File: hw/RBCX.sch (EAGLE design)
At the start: 477 parts, among them IC1 AMS1117-3.3, IC10 INA180A4, IC11 INA180A4, IC12 MPU-6050, IC13 STM32F103VCT6, IC2 DRV8833PWP, IC3 INA180A4, IC4 INA180A4, IC5 DRV8833PWP, IC6 INA180A4, IC7 INA180A4, IC8 INA180A4, IC9 INA180A4, P1 M1, P2 M2, P3 M3, P4 M4, Q1 NCE20P45Q, Q10 2N7002, Q2 NCE20P45Q, Q3 2N7002, Q4 2N7002, Q5 2N7002, Q6 2N7002, Q7 2N7002, Q8 2N7002, Q9 2N7002, X1 POWER_IN, X2 POWER_OUT, X3 52559-3092, X4 uUSB, Y1 5032/2P, Y2 3215_2P

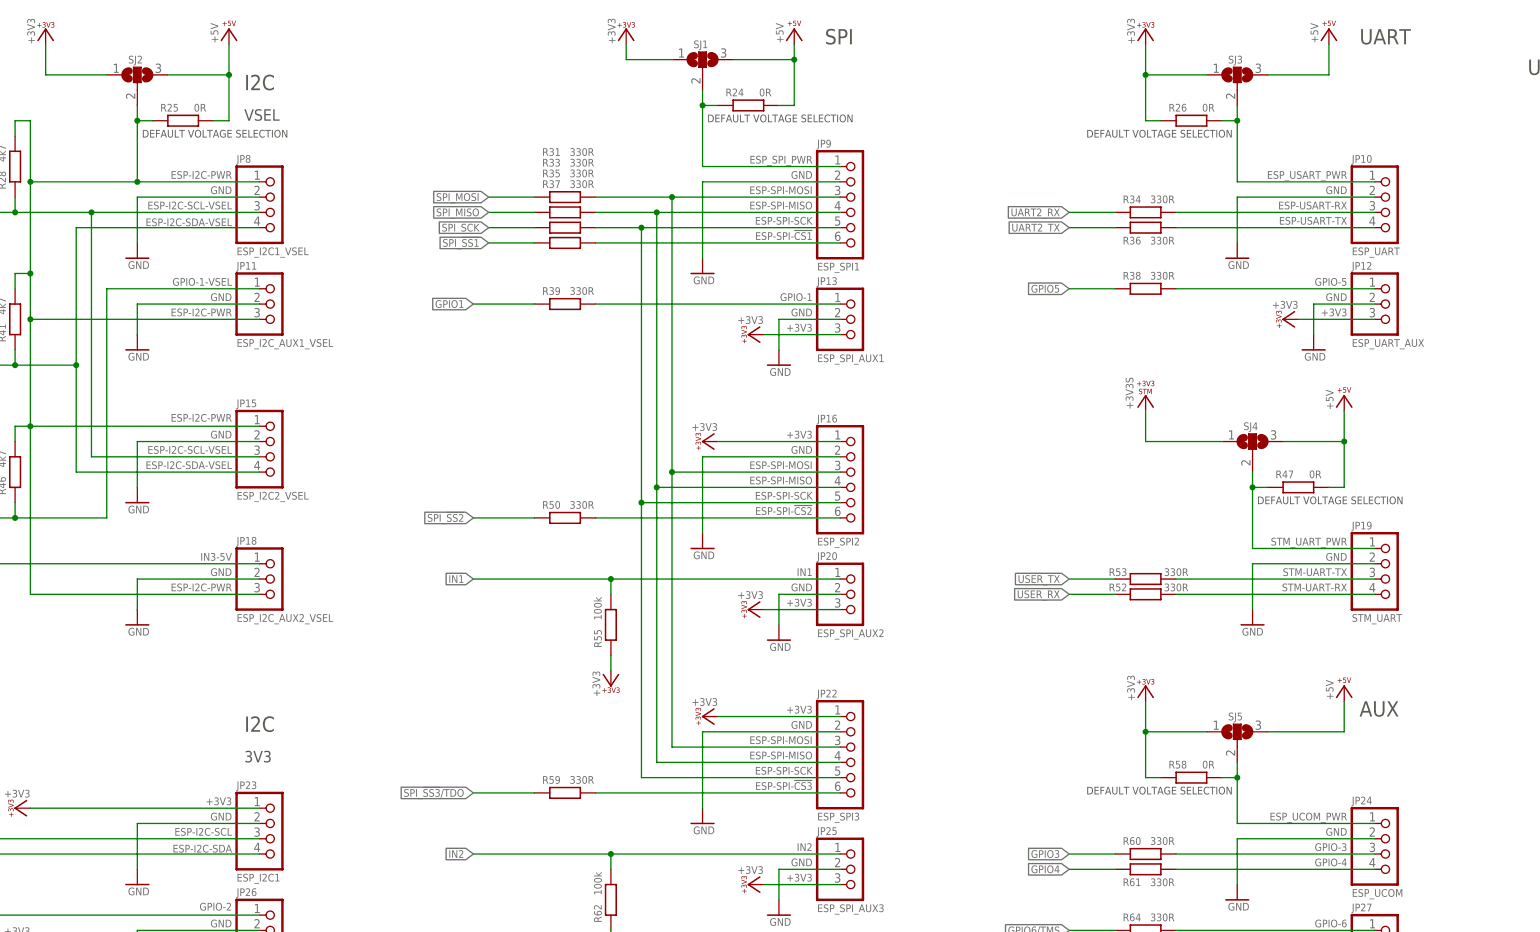
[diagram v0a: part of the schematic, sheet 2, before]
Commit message: hw: jumpers modified to match 0603 resistors
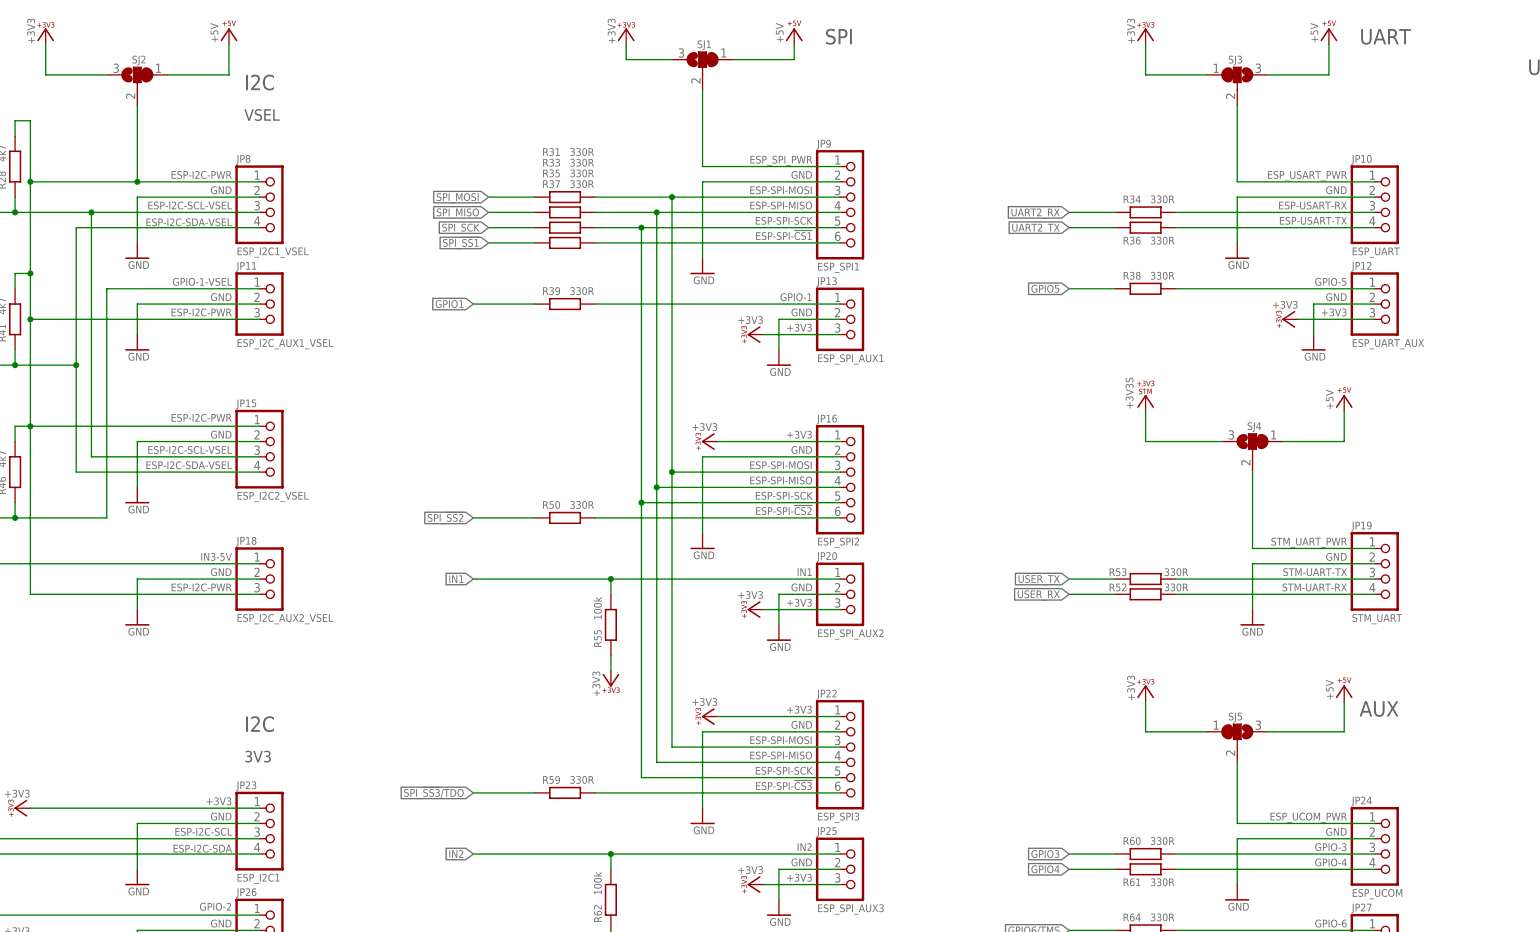
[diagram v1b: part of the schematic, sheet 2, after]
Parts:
- removed R119, R126, R24, R25, R26, R47, R58: 0R, rcl_upravena:R-EU_R0603
- SJ1, SJ2, SJ3, SJ4, SJ5, SJ8, SJ9: device jumper:SJ2W -> jumper:SJ2W_DEFAULT
- SJ6, SJ7: device jumper:SJ2W -> jumper:SJ2W0603
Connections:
- net +3V3: now also SJ1.3, SJ2.3; no longer R26.1, R58.1, SJ1.1, SJ2.1
- net +3V3S: now also SJ4.3; no longer R119.1, R126.1, SJ4.1
- net +5V: now also SJ1.1, SJ2.1, SJ4.1; no longer R24.2, R25.2, R47.2, SJ1.3, SJ2.3, SJ4.3
- net ENC12_PWR: no longer R119.2
- net ENC34_PWR: no longer R126.2
- net ESP-I2C-PWR: no longer R25.1
- net ESP_SPI_PWR: no longer R24.1
- net ESP_UCOM_PWR: no longer R58.2
- net ESP_USART_PWR: no longer R26.2
- net STM_UART_PWR: no longer R47.1
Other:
- note removed: "DEFAULT VOLTAGE SELECTION"

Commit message: hw: renumber parts
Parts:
- removed R158, R159, R160, R163, R164: 330R, rcl_upravena:R-EU_R0402
- removed R161, R162: 4k7, rcl_upravena:R-EU_R0402
- removed TP62: (no value), test_points:TP_06MM
- added R119, R126: 5m, rcl_upravena:R-EU_R1206
- added R24, R25: 4k7, rcl_upravena:R-EU_R0402
- added R26, R47, R58: 330R, rcl_upravena:R-EU_R0402
- added TP21: (no value), test_points:TP_06MM
- D11, D13, D26, D27, D28: value BAS40-04 -> BAS40-05; device diode:BAS40-04 -> diode:BAS40-05
- D12, D29, D30: value BAS40-04 -> SS34; device diode:BAS40-04 -> diode:SHOTTKY-SMA
- D14, D20: value BAS40-04 -> B5819W; device diode:BAS40-04 -> diode:SHOTTKY-SOD123; DESCRIPTION (none) -> 40V 1A 600mV @ 1A SOD-123 Schottky Barrier Diodes (SBD) RoHS; EXTENDED (none) -> NO; LCSC_ID (none) -> C305445; MF (none) -> Foshan Blue Rocket Elec; MF_ID (none) -> B5819W; PACKAGE (none) -> SOD-123; PADS (none) -> 2; PRICE_100PLUS (none) -> $0.0176; PRICE_1PLUS (none) -> $0.0342; PRICE_DATE (none) -> 17.03.2020
- D16, D35, D36, D37: value BAS40-05 -> BAS40-04; device diode:BAS40-05 -> diode:BAS40-04
- D22, D23, D24, D25, D33: value SS34 -> BAS40-04; device diode:SHOTTKY-SMA -> diode:BAS40-04
- D38: value BAS40-05 -> SS34; device diode:BAS40-05 -> diode:SHOTTKY-SMA
- D7: value B5819W -> SS34; device diode:SHOTTKY-SOD123 -> diode:SHOTTKY-SMA; DESCRIPTION 40V 1A 600mV @ 1A SOD-123 Schottky Barrier Diodes (SBD) RoHS -> (none); EXTENDED NO -> (none); LCSC_ID C305445 -> (none); MF Foshan Blue Rocket Elec -> (none); MF_ID B5819W -> (none); PACKAGE SOD-123 -> (none); PADS 2 -> (none); PRICE_100PLUS $0.0176 -> (none); PRICE_1PLUS $0.0342 -> (none); PRICE_DATE 17.03.2020 -> (none)
- D9: value B5819W -> BAS40-04; device diode:SHOTTKY-SOD123 -> diode:BAS40-04; DESCRIPTION 40V 1A 600mV @ 1A SOD-123 Schottky Barrier Diodes (SBD) RoHS -> (none); EXTENDED NO -> (none); LCSC_ID C305445 -> (none); MF Foshan Blue Rocket Elec -> (none); MF_ID B5819W -> (none); PACKAGE SOD-123 -> (none); PADS 2 -> (none); PRICE_100PLUS $0.0176 -> (none); PRICE_1PLUS $0.0342 -> (none); PRICE_DATE 17.03.2020 -> (none)
- JP10: value ESP_UART -> ESP_I2C_AUX1_VSEL; device pinhead:PINHD-1X4 -> pinhead:PINHD-1X3
- JP11: value ESP_I2C_AUX1_VSEL -> ESP_UART_AUX
- JP12: value ESP_UART_AUX -> ESP_SPI_AUX1
- JP13: value ESP_SPI_AUX1 -> UTS2; device pinhead:PINHD-1X3 -> pinhead:PINHD-1X4
- JP14: value UTS2 -> ESP_I2C2_VSEL
- JP15: value ESP_I2C2_VSEL -> ESP_SPI2; device pinhead:PINHD-1X4 -> pinhead:PINHD-1X6
- JP16: value ESP_SPI2 -> UTS3; device pinhead:PINHD-1X6 -> pinhead:PINHD-1X4
- JP17: value UTS3 -> ESP_I2C_AUX2_VSEL; device pinhead:PINHD-1X4 -> pinhead:PINHD-1X3
- JP18: value ESP_I2C_AUX2_VSEL -> STM_UART; device pinhead:PINHD-1X3 -> pinhead:PINHD-1X4
- JP19: value STM_UART -> ESP_SPI_AUX2; device pinhead:PINHD-1X4 -> pinhead:PINHD-1X3
- JP20: value ESP_SPI_AUX2 -> UTS4; device pinhead:PINHD-1X3 -> pinhead:PINHD-1X4
- JP21: value UTS4 -> ESP_SPI3; device pinhead:PINHD-1X4 -> pinhead:PINHD-1X6
- JP22: value ESP_SPI3 -> ESP_I2C1; device pinhead:PINHD-1X6 -> pinhead:PINHD-1X4
- JP23: value ESP_I2C1 -> ESP_UCOM
- JP24: value ESP_UCOM -> ESP_SPI_AUX3; device pinhead:PINHD-1X4 -> pinhead:PINHD-1X3
- JP25: value ESP_SPI_AUX3 -> ESP_I2C_AUX1
- JP26: value ESP_I2C_AUX1 -> ESP_UCOM_AUX
- JP27: value ESP_UCOM_AUX -> ILED_EN; device pinhead:PINHD-1X3 -> pinhead:PINHD-1X1
- JP29: value ILED_EN -> AIO; device pinhead:PINHD-1X1 -> pinhead:PINHD-2X4
- JP30: value AIO -> ESP_I2C_AUX2; device pinhead:PINHD-2X4 -> pinhead:PINHD-1X3
- JP31: value ESP_I2C_AUX2 -> ILED
- JP32: value ILED -> USB; device pinhead:PINHD-1X3 -> pinhead:PINHD-1X5
- JP33: value USB -> SWD; device pinhead:PINHD-1X5 -> pinhead:PINHD-1X6
- JP34: value SWD -> DEBUG; device pinhead:PINHD-1X6 -> pinhead:PINHD-1X4
- JP35: value DEBUG -> USBC_AUX
- JP4: value BUZZER -> +5V; device pinhead:PINHD-1X1 -> pinhead:PINHD-2X4
- JP42: value BUTTONS -> LEDS
- JP43: value LEDS -> BUTTONS
- JP44: value PWR_BUTTONS -> BUZZER; device pinhead:PINHD-2X4 -> pinhead:PINHD-1X1
- JP45: value M12FAULT -> PWR_BUTTONS; device pinhead:PINHD-1X1 -> pinhead:PINHD-2X4
- JP46: value M34FAULT -> M12FAULT
- JP47: value SERVO1_EN -> M34FAULT
- JP48: value SERVO2_EN -> SERVO1_EN
- JP49: value SERVO3_EN -> SERVO2_EN
- JP5: value +5V -> VCC
- JP50: value SERVO4_EN -> SERVO3_EN
- JP51: value SERVO1 -> SERVO4_EN; device pinhead:PINHD-1X3 -> pinhead:PINHD-1X1
- JP52: value SERVO2 -> SERVO1
- JP53: value SERVO3 -> SERVO2
- JP54: value SERVO4 -> SERVO3
- JP55: value INTELIGENT_SERVO1 -> SERVO4; device iServo_connector:292161-3 -> pinhead:PINHD-1X3; DESCRIPTION Connector for inteligent servo LewanSoul (e.g. LX-15D) -> (none); PACKAGE 292161-3 -> (none)
- JP56: value INTELIGENT_SERVO2 -> INTELIGENT_SERVO1
- JP57: value I2C_INTERCONNECT -> INTELIGENT_SERVO2; device pinhead:PINHD-2X2 -> iServo_connector:292161-3; DESCRIPTION (none) -> Connector for inteligent servo LewanSoul (e.g. LX-15D); PACKAGE (none) -> 292161-3
- JP58: value USBC_AUX -> I2C_INTERCONNECT; device pinhead:PINHD-1X4 -> pinhead:PINHD-2X2
- JP6: value VCC -> UTS1; device pinhead:PINHD-2X4 -> pinhead:PINHD-1X4
- JP7: value UTS1 -> ESP_I2C1_VSEL
- JP8: value ESP_I2C1_VSEL -> ESP_SPI1; device pinhead:PINHD-1X4 -> pinhead:PINHD-1X6
- JP9: value ESP_SPI1 -> ESP_UART; device pinhead:PINHD-1X6 -> pinhead:PINHD-1X4
- R102: value 330R -> 2k2
- R105, R147, R148, R149, R150, R151: value 2k2 -> 330R
- R107, R109: value 330R -> 1M
- R110, R111, R154, R155, R37, R38, R42, R43, R50, R64, R78: value 330R -> 4k7
- R112: value 1M -> 1k
- R113, R77: value 330R -> 1k
- R114: value 1M -> 2k2
- R115, R116: value 4k7 -> 2k2
- R117, R141, R143: value 1k -> 2k2
- R118, R139: value 1k -> 5m; device rcl_upravena:R-EU_R0402 -> rcl_upravena:R-EU_R1206
- R124, R125: value 5m -> 10k; device rcl_upravena:R-EU_R1206 -> rcl_upravena:R-EU_R0402
- R127: value 2k2 -> 5m; device rcl_upravena:R-EU_R0402 -> rcl_upravena:R-EU_R1206
- R128, R129, R130: value 2k2 -> 0R; device rcl_upravena:R-EU_R0402 -> rcl_upravena:R-EU_R1206
- R131: value 10k -> 0R; device rcl_upravena:R-EU_R0402 -> rcl_upravena:R-EU_R1206
- R132, R76: value 10k -> 1k
- R134: value 5m -> 1k; device rcl_upravena:R-EU_R1206 -> rcl_upravena:R-EU_R0402
- R135, R137: value 0R -> 5m
- R136, R138: value 0R -> 1k; device rcl_upravena:R-EU_R1206 -> rcl_upravena:R-EU_R0402
- R140, R142, R144: value 5m -> 2k2; device rcl_upravena:R-EU_R1206 -> rcl_upravena:R-EU_R0402
- R145, R81, R82: value 1k -> 330R
- R146: value 5m -> 330R; device rcl_upravena:R-EU_R1206 -> rcl_upravena:R-EU_R0402
- R27, R28, R40, R41, R45, R46, R54, R69, R83, R84: value 4k7 -> 330R
- R51, R57, R74: value 330R -> 100k
- R55, R80: value 100k -> 330R
- R62, R79: value 100k -> 4k7
- R63: value 330R -> 0R; device rcl_upravena:R-EU_R0402 -> rcl_upravena:R-EU_R1206
- R67: value 4k7 -> 1k5; EXTENDED (none) -> NO; LCSC_ID (none) -> C25867; MF (none) -> Uniroyal Elec; MF_ID (none) -> 0402WGF1501TCE; PACKAGE (none) -> R0402; PADS (none) -> 2; PRICE_1000PLUS (none) -> 0.0003; PRICE_1PLUS (none) -> 0.0009
- R68: value 0R -> 330R; device rcl_upravena:R-EU_R1206 -> rcl_upravena:R-EU_R0402
- R70: value 330R -> 5k6
- R71: value 330R -> 10k
- R72: value 1k5 -> 330R; EXTENDED NO -> (none); LCSC_ID C25867 -> (none); MF Uniroyal Elec -> (none); MF_ID 0402WGF1501TCE -> (none); PACKAGE R0402 -> (none); PADS 2 -> (none); PRICE_1000PLUS 0.0003 -> (none); PRICE_1PLUS 0.0009 -> (none)
- R75: value 5k6 -> 100k
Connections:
- net !M12_FAULT: now also JP46.1; no longer JP45.1
- net !M34_FAULT: now also JP47.1; no longer JP46.1
- net +3V3: now also JP11.3, JP15.1, JP19.3, JP21.1, JP24.3, JP30.3, R24.2, R37.2, R42.2, R50.1, R51.1, R57.1; no longer JP13.3, JP16.1, JP20.3, JP23.1, JP27.3, JP31.3, R27.2, R40.2, R45.2, R54.1, R55.1, R67.1
- net +3V3S: now also D11.C, D13.C, D16.C2, D22.C2, D23.C2, D24.C2, D25.C2, D27.C, D28.C, D33.C2, D35.C2, D36.C2, D37.C2, D9.C2, JP29.5, JP29.6, JP33.1, R107.2, R154.2, R155.2, R78.2, R79.2; no longer D11.C2, D12.C2, D13.C2, D14.C2, D20.C2, D26.C2, D27.C2, D28.C2, D29.C2, D30.C2, D35.C, D36.C, D37.C, D38.C, JP30.5, JP30.6, JP35.1, R112.2, R161.2, R162.2, R83.2, R84.2
- net +5V: now also D1.A, D12.C, D14.C, D38.A, D5.C, D6.A, JP13.1, JP16.1, JP20.1, JP29.7, JP29.8, JP4.1, JP4.3, JP4.5, JP4.7, JP6.1, R128.1, R63.2; no longer D3.C, D31.A, D32.A, D4.A, D8.C, D9.C, JP14.1, JP17.1, JP21.1, JP30.7, JP30.8, JP5.1, JP5.3, JP5.5, JP5.7, JP7.1, R135.1, R68.2
- net 3V3_EN: now also D11.A2; no longer D38.A2
- net 3V3_IN: now also D6.C, D7.C; no longer D4.C, D5.C
- net 5V_IN: now also D4.C; no longer D2.C
- net BAT+_PROTECTED: now also D1.C, D2.C; no longer D32.C, D33.C
- net BOOT0: now also R75.1; no longer R80.1
- net BOOT1_PULL-DOWN: now also R74.1; no longer R79.1
- net BUTTON-1: now also JP43.1, R90.2, S3.S, S3.S1, S4.S, S4.S1; no longer JP42.1, R97.2, S2.S, S2.S1, S8.S, S8.S1
- net BUTTON-2: now also JP43.3, R93.2, S5.S, S5.S1, S6.S, S6.S1; no longer JP42.3, R99.2, S3.S, S3.S1, S9.S, S9.S1
- net BUTTON-3: now also JP43.5, R74.2, R96.2, S7.S, S7.S1, S8.S, S8.S1; no longer JP42.5, R101.2, R79.2, S10.S, S10.S1, S4.S, S4.S1
- net BUTTON-4: now also JP43.7, R100.2, S10.S, S10.S1, S9.S, S9.S1; no longer JP42.7, R103.2, S11.S, S11.S1, S5.S, S5.S1
- net BUTTON-OFF: now also JP45.1, R102.2, S11.S, S11.S1; no longer JP44.1, R105.2, S6.S, S6.S1
- net BUTTON-ON: now also JP45.3, S2.S, S2.S1; no longer JP44.3, S14.S, S14.S1
- net BUTTON1: now also R90.1; no longer R97.1
- net BUTTON2: now also R93.1; no longer R99.1
- net BUTTON3: now also R96.1; no longer R101.1
- net BUTTON4: now also R100.1; no longer R103.1
- net BUTTON_OFF: now also D13.A1, R102.1; no longer D35.A1, R105.1
- net BUZZER: now also R108.1; no longer R113.1
- net BUZZER-: now also D14.A; no longer D9.A
- net BUZZER-GATE: now also JP44.1, R108.2, R109.1; no longer JP4.1, R113.2, R114.1
- net CONTROL-DIR: now also R84.2; no longer R89.2
- net CONTROL-INT: now also R85.2; no longer R90.2
- net CONTROL-RX/SDA: now also R83.2; no longer R88.2
- net CONTROL-TX/SCL: now also R82.2; no longer R87.2
- net CONTROL_RX/SDA: now also R145.2, R83.1; no longer R152.2, R88.1
- net CONTROL_TX/SCL: now also R146.2, R82.1; no longer R153.2, R87.1
- net DEBUG-RX: now also JP34.3, R72.2; no longer JP35.3, R77.2
- net DEBUG-TX: now also JP34.4, R73.2; no longer JP35.4, R78.2
- net DEBUG_RX: now also R72.1; no longer R77.1
- net DEBUG_TX: now also R73.1; no longer R78.1
- net ENC12PWR: now also D15.C, TP21.TP; no longer D10.C, TP22.TP
- net ENC12_PWR: now also D15.A; no longer D10.A
- net ENC1A: now also D16.C1A2, R114.1, TP26.TP; no longer D11.C1A2, R120.1, TP27.TP
- net ENC1B: now also D17.C1A2, R115.1, TP27.TP; no longer D12.C1A2, R121.1, TP28.TP
- net ENC2A: now also D18.C1A2, R116.1, TP28.TP; no longer D13.C1A2, R122.1, TP29.TP
- net ENC2B: now also D19.C1A2, R117.1, TP29.TP; no longer D14.C1A2, R123.1, TP30.TP
- net ENC34PWR: now also D20.C, TP32.TP; no longer D15.C, TP33.TP
- net ENC34_PWR: now also D20.A; no longer D15.A
- net ENC3A: now also D22.C1A2, R120.1, TP40.TP; no longer D17.C1A2, R127.1, TP41.TP
- net ENC3B-SWO: now also R69.2; no longer R74.2
- net ENC3B/SWO: now also D23.C1A2, R121.1, R69.1, TP41.TP; no longer D18.C1A2, R128.1, R74.1, TP42.TP
- net ENC4A: now also D24.C1A2, R122.1, TP42.TP; no longer D19.C1A2, R129.1, TP43.TP
- net ENC4B: now also D25.C1A2, R123.1, TP43.TP; no longer D20.C1A2, R130.1, TP44.TP
- net ENC_1A: now also R114.2; no longer R120.2
- net ENC_1B: now also R115.2; no longer R121.2
- net ENC_2A: now also R116.2; no longer R122.2
- net ENC_2B: now also R117.2; no longer R123.2
- net ENC_3A: now also R120.2; no longer R127.2
- net ENC_3B: now also R121.2; no longer R128.2
- net ENC_4A: now also R122.2; no longer R129.2
- net ENC_4B: now also R123.2; no longer R130.2
- net ESP-I2C-PWR: now also JP10.3, JP14.1, JP17.3, JP7.1, R25.2, R38.2, R43.2; no longer JP11.3, JP15.1, JP18.3, JP8.1, R28.2, R41.2, R46.2
- net ESP-I2C-SCL: now also JP22.3, JP58.3, R24.1, R29.2; no longer JP23.3, JP57.3, R27.1, R32.2
- net ESP-I2C-SCL-VSEL: now also JP14.3, JP7.3, R25.1; no longer JP15.3, JP8.3, R28.1
- net ESP-I2C-SDA: now also JP22.4, JP58.1, R37.1, R41.2; no longer JP23.4, JP57.1, R40.1, R44.2
- net ESP-I2C-SDA-VSEL: now also JP14.4, JP7.4, R38.1; no longer JP15.4, JP8.4, R41.1
- net ESP-SPI-!CS1: now also JP8.6, R34.2; no longer JP9.6, R37.2
- net ESP-SPI-!CS2: now also JP15.6, R46.2; no longer JP16.6, R50.2
- net ESP-SPI-!CS3: now also JP21.6, R54.2; no longer JP22.6, R59.2
- net ESP-SPI-MISO: now also JP15.4, JP21.4, JP8.4, R30.2; no longer JP16.4, JP22.4, JP9.4, R33.2
- net ESP-SPI-MOSI: now also JP15.3, JP21.3, JP8.3, R28.2; no longer JP16.3, JP22.3, JP9.3, R31.2
- net ESP-SPI-SCK: now also JP15.5, JP21.5, JP8.5, R32.2; no longer JP16.5, JP22.5, JP9.5, R35.2
- net ESP-UART-RX: now also R87.2; no longer R92.2
- net ESP-UART-TX: now also R86.2; no longer R91.2
- net ESP-USART-RX: now also JP9.3, R31.2; no longer JP10.3, R34.2
- net ESP-USART-TX: now also JP9.4, R33.2; no longer JP10.4, R36.2
- net ESP_+5V: now also D38.C, D8.C, TP60.TP; no longer D31.C, D6.C, TP61.TP
- net ESP_EN: now also D13.A2, JP45.5, R107.1, S14.S, S14.S1, TP59.TP; no longer D35.A2, JP44.5, R112.1, S7.S, S7.S1, TP60.TP
- net ESP_SPI_PWR: now also JP8.1; no longer JP9.1
- net ESP_UCOM_PWR: now also JP23.1; no longer JP24.1
- net ESP_USART_PWR: now also JP9.1; no longer JP10.1
- net EXPANDER_COM_PWR: now also D12.A; no longer D8.A
- net EXPANDER_RX: now also R146.1; no longer R153.1
- net EXPANDER_TX: now also R145.1; no longer R152.1
- net GND: now also D16.A1, D22.A1, D23.A1, D24.A1, D25.A1, D3.A, D33.A1, D35.A1, D36.A1, D37.A1, D9.A1, JP13.4, JP14.2, JP16.4, JP17.2, JP20.4, JP21.2, JP29.3, JP29.4, JP30.2, JP31.3, JP32.5, JP33.3, JP34.2, JP4.2, JP4.4, JP4.6, JP4.8, JP45.2, JP45.4, JP45.6, JP45.8, JP57.3, JP7.2, R109.2, R110.1, R111.1, R112.1, R113.1, R119.1, R126.1, R127.1, R71.1, R75.2, R76.2, R77.2; no longer D1.A, D11.A1, D12.A1, D13.A1, D14.A1, D20.A1, D26.A1, D27.A1, D28.A1, D29.A1, D30.A1, JP13.2, JP14.4, JP16.2, JP17.4, JP20.2, JP21.4, JP27.2, JP30.3, JP30.4, JP31.2, JP32.3, JP33.5, JP34.3, JP35.2, JP44.2, JP44.4, JP44.6, JP44.8, JP51.3, JP6.2, JP6.6, JP6.8, JP7.4, R114.2, R115.1, R116.1, R117.1, R131.1, R132.1, R133.1, R134.1, R76.1, R80.2, R81.2, R82.2
- net GPIO-1: now also JP12.1, R36.2; no longer JP13.1, R39.2
- net GPIO-1-VSEL: now also JP10.1, R43.1; no longer JP11.1, R46.1
- net GPIO-2: now also JP25.1, R58.2; no longer JP26.1, R63.2
- net GPIO-3: now also JP23.3, R55.2; no longer JP24.3, R60.2
- net GPIO-4: now also JP23.4, R56.2; no longer JP24.4, R61.2
- net GPIO-5: now also JP11.1, R35.2; no longer JP12.1, R38.2
- net GPIO-6: now also JP26.1, R59.2; no longer JP27.1, R64.2
- net GPIO-7: now also R42.1, R45.2; no longer R45.1, R49.2
- net GPIO1: now also R36.1; no longer R39.1
- net GPIO2: now also R58.1; no longer R63.1
- net GPIO3: now also R55.1; no longer R60.1
- net GPIO4: now also R56.1; no longer R61.1
- net GPIO5: now also R35.1; no longer R38.1
- net GPIO6/TMS: now also R149.1, R59.1; no longer R156.1, R64.1
- net GPIO7/TCK: now also R150.1, R45.1; no longer R157.1, R49.1
- net I2C_SCL: now also R29.1; no longer R32.1
- net I2C_SDA: now also R41.1; no longer R44.1
- net ILED: now also R65.2; no longer R70.2
- net ILED-5V: now also JP31.1, R64.1; no longer JP32.1, R69.1
- net ILED_EN: now also D11.A1, JP27.1; no longer D38.A1, JP29.1
- net ILED_PWR: now also JP31.2, R63.1, R64.2; no longer JP32.2, R68.1, R69.2
- net IN1: now also JP19.1, R51.2; no longer JP20.1, R55.2
- net IN2: now also JP24.1, R57.2; no longer JP25.1, R62.2
- net IN3: now also D10.A, R50.2; no longer D7.A, R54.2
- net IN3-5V: now also D10.C, JP17.1; no longer D7.C, JP18.1
- net IN4: now also JP30.1, R62.2; no longer JP31.1, R67.2
- net IN4A: now also D21.A1, TP35.TP; no longer D16.A1, TP36.TP
- net IN4B: now also D26.A2, TP37.TP; no longer D21.A2, TP38.TP
- net IN4_A: now also D21.C, R125.2, TP38.TP; no longer D16.C, R132.2, TP39.TP
- net IN4_B: now also D26.C, R124.2, TP39.TP; no longer D21.C, R131.2, TP40.TP
- net INTELLIGENT_SERVO: now also D37.C1A2, R144.1, TP58.TP; no longer D30.C1A2, R151.1, TP59.TP
- net ISERVO: now also JP57.1, R144.2; no longer JP55.1, R151.2
- net I_LED/TDI: now also R151.1, R65.1; no longer R158.1, R70.1
- net LED-1: now also JP42.1, R103.2; no longer JP43.1, R108.2
- net LED-2: now also JP42.3, R104.2; no longer JP43.3, R109.2
- net LED-3: now also JP42.5, R105.2; no longer JP43.5, R110.2
- net LED-4: now also JP42.7, R106.2; no longer JP43.7, R111.2
- net LED1: now also R103.1, R91.1, R92.1; no longer R108.1, R95.1, R96.1
- net LED2: now also R104.1, R94.1, R95.1; no longer R100.1, R109.1, R98.1
- net LED3: now also R105.1, R97.1, R98.1; no longer R102.1, R104.1, R110.1
- net LED4: now also R101.1, R99.1; no longer R107.1, R111.1
- net LED_1: now also R91.2; no longer R95.2
- net LED_1B: now also R92.2; no longer R96.2
- net LED_2: now also R94.2; no longer R98.2
- net LED_2B: now also R95.2; no longer R100.2
- net LED_3: now also R97.2; no longer R102.2
- net LED_3B: now also R98.2; no longer R104.2
- net LED_4: now also R99.2; no longer R106.2
- net LED_4B: now also R101.2; no longer R107.2
- net M1GND: now also R118.2; no longer R124.2
- net M2GND: now also R119.2; no longer R125.2
- net M3GND: now also R126.2; no longer R133.2
- net M4GND: now also R127.2; no longer R134.2
- net MI1: now also TP30.TP; no longer TP31.TP
- net MI2: now also TP31.TP; no longer TP32.TP
- net MI3: now also TP44.TP; no longer TP45.TP
- net MI4: now also TP45.TP; no longer TP46.TP
- net MPU-INT: now also R153.2; no longer R160.2
- net MPU-SCL: now also R78.1, R80.1; no longer R83.1, R85.1
- net MPU-SDA: now also R79.1, R81.1; no longer R84.1, R86.1
- net MPU_INT: now also R153.1, TP61.TP; no longer R160.1, TP62.TP
- net MPU_SCL: now also R80.2; no longer R85.2
- net MPU_SDA: now also R81.2; no longer R86.2
- net NRST: now also JP33.5, JP45.7; no longer JP34.5, JP44.7
- net PWM1A: now also TP23.TP; no longer TP24.TP
- net PWM1B: now also TP22.TP; no longer TP23.TP
- net PWM2A: now also TP25.TP; no longer TP26.TP
- net PWM2B: now also TP24.TP; no longer TP25.TP
- net PWM3A: now also TP33.TP; no longer TP34.TP
- net PWM3B: now also TP34.TP; no longer TP35.TP
- net PWM4: now also D21.A2, D26.A1, TP36.TP; no longer D16.A2, D21.A1, TP37.TP
- net PWRLED_+3V3S1: now also R112.2; no longer R117.2
- net PWRLED_+3V3S_B1: now also R113.2; no longer R118.2
- net PWRLED_VCC1: now also R110.2; no longer R115.2
- net PWRLED_VCC_B1: now also R111.2; no longer R116.2
- net SERVO1: now also D33.C1A2, R140.1, TP54.TP; no longer D26.C1A2, R147.1, TP55.TP
- net SERVO1PWR: now also D29.A, R128.2, R129.1; no longer D22.A, R135.2, R136.1
- net SERVO1_EN: now also D27.A2, JP48.1; no longer D36.A2, JP47.1
- net SERVO1_PWR: now also D29.C, R133.2; no longer D22.C, R140.2
- net SERVO2: now also D34.C1A2, R141.1, TP55.TP; no longer D27.C1A2, R148.1, TP56.TP
- net SERVO2PWR: now also D30.A, R129.2, R130.1; no longer D23.A, R136.2, R137.1
- net SERVO2_EN: now also D27.A1, JP49.1; no longer D36.A1, JP48.1
- net SERVO2_PWR: now also D30.C, R135.2; no longer D23.C, R142.2
- net SERVO3: now also D35.C1A2, R142.1, TP56.TP; no longer D28.C1A2, R149.1, TP57.TP
- net SERVO3PWR: now also D31.A, R130.2, R131.1; no longer D24.A, R137.2, R138.1
- net SERVO3_EN: now also D28.A2, JP50.1; no longer D37.A2, JP49.1
- net SERVO3_PWR: now also D31.C, R137.2; no longer D24.C, R144.2
- net SERVO4: now also D36.C1A2, R143.1, TP57.TP; no longer D29.C1A2, R150.1, TP58.TP
- net SERVO4PWR: now also D32.A, R131.2; no longer D25.A, R138.2
- net SERVO4_EN: now also D28.A1, JP51.1; no longer D37.A1, JP50.1
- net SERVO4_PWR: now also D32.C, R139.2; no longer D25.C, R146.2
- net SERVO_1: now also JP52.1, R140.2; no longer JP51.1, R147.2
- net SERVO_1_PWR: now also JP52.2, R133.1, TP50.TP; no longer JP51.2, R140.1, TP51.TP
- net SERVO_2: now also JP53.1, R141.2; no longer JP52.1, R148.2
- net SERVO_2_PWR: now also JP53.2, R135.1, TP51.TP; no longer JP52.2, R142.1, TP52.TP
- net SERVO_3: now also JP54.1, R142.2; no longer JP53.1, R149.2
- net SERVO_3_PWR: now also JP54.2, R137.1, TP52.TP; no longer JP53.2, R144.1, TP53.TP
- net SERVO_4: now also JP55.1, R143.2; no longer JP54.1, R150.2
- net SERVO_4_PWR: now also JP55.2, R139.1, TP53.TP; no longer JP54.2, R146.1, TP54.TP
- net SI1: now also R132.1, TP46.TP; no longer R139.1, TP47.TP
- net SI2: now also R134.1, TP47.TP; no longer R141.1, TP48.TP
- net SI3: now also R136.1, TP48.TP; no longer R143.1, TP49.TP
- net SI4: now also R138.1, TP49.TP; no longer R145.1, TP50.TP
- net SI_1: now also R132.2; no longer R139.2
- net SI_2: now also R134.2; no longer R141.2
- net SI_3: now also R136.2; no longer R143.2
- net SI_4: now also R138.2; no longer R145.2
- net SPI_!SS1: now also R34.1; no longer R37.1
- net SPI_!SS2: now also R46.1; no longer R50.1
- net SPI_!SS3!/TDO: now also R152.1, R54.1; no longer R159.1, R59.1
- net SPI_MISO: now also R30.1; no longer R33.1
- net SPI_MOSI: now also R28.1; no longer R31.1
- net SPI_SCK: now also R32.1; no longer R35.1
- net STM-AIO1: now also JP29.1, R60.2; no longer JP30.1, R65.2
- net STM-AIO2: now also JP29.2, R61.1; no longer JP30.2, R66.1
- net STM-CAN-RX: now also R89.2; no longer R94.2
- net STM-CAN-TX: now also R88.2; no longer R93.2
- net STM-I2C-SCL: now also JP58.4, R155.1, R157.2; no longer JP57.4, R162.1, R164.2
- net STM-I2C-SDA: now also JP58.2, R154.1, R156.2; no longer JP57.2, R161.1, R163.2
- net STM-UART-RX: now also JP18.4, R49.2; no longer JP19.4, R53.2
- net STM-UART-TX: now also JP18.3, R48.2; no longer JP19.3, R52.2
- net STM_AIO1: now also R60.1; no longer R65.1
- net STM_AIO2: now also R61.2; no longer R66.2
- net STM_CAN_RX: now also R89.1; no longer R94.1
- net STM_CAN_TX: now also R88.1; no longer R93.1
- net STM_I2C_SCL: now also R157.1; no longer R164.1
- net STM_I2C_SDA: now also R156.1; no longer R163.1
- net STM_SPI_!CS: now also R149.2, R84.1; no longer R156.2, R89.1
- net STM_SPI_MISO: now also R152.2, R85.1; no longer R159.2, R90.1
- net STM_SPI_MOSI: now also R151.2; no longer R158.2
- net STM_SPI_SCK: now also R150.2; no longer R157.2
- net STM_UART_PWR: now also JP18.1; no longer JP19.1
- net SWCLK: now also R66.1; no longer R71.1
- net SWCLK_: now also JP33.2, R66.2; no longer JP34.2, R71.2
- net SWDIO: now also R68.1; no longer R73.1
- net SWDIO_: now also JP33.4, R68.2; no longer JP34.4, R73.2
- net SWO: now also JP33.6; no longer JP34.6
- net TUNNEL_RX: now also R147.2; no longer R154.2
- net TUNNEL_TX: now also R148.2; no longer R155.2
- net UART2_RX: now also R31.1; no longer R34.1
- net UART2_TX: now also R33.1; no longer R36.1
- net UART_RX: now also R148.1, R87.1; no longer R155.1, R92.1
- net UART_TX: now also R147.1, R86.1; no longer R154.1, R91.1
- net USB_CC1: now also JP35.2, R77.1; no longer JP58.2, R82.1
- net USB_CC2: now also JP35.4, R76.1; no longer JP58.4, R81.1
- net USB_DM: now also JP32.2; no longer JP33.2
- net USB_DP: now also JP32.3, R67.2; no longer JP33.3, R72.2
- net USB_DP_PULLUP: now also R67.1; no longer R72.1
- net USB_ID: now also JP32.4; no longer JP33.4
- net USB_SBU1: now also JP35.1; no longer JP58.1
- net USB_SBU2: now also JP35.3; no longer JP58.3
- net USER_RX: now also R49.1; no longer R53.1
- net USER_TX: now also R48.1; no longer R52.1
- net UTS1-ECHO: now also JP6.3, R27.2; no longer JP7.3, R30.2
- net UTS1-TRIG: now also JP6.2, R26.2; no longer JP7.2, R29.2
- net UTS1_ECHO: now also R27.1; no longer R30.1
- net UTS1_TRIG: now also R26.1; no longer R29.1
- net UTS2-ECHO: now also JP13.3, R40.2; no longer JP14.3, R43.2
- net UTS2-TRIG: now also JP13.2, R39.2; no longer JP14.2, R42.2
- net UTS2_ECHO: now also R40.1; no longer R43.1
- net UTS2_TRIG: now also R39.1; no longer R42.1
- net UTS3-ECHO: now also JP16.3, R47.2; no longer JP17.3, R51.2
- net UTS3-TRIG: now also JP16.2, R44.2; no longer JP17.2, R48.2
- net UTS3_ECHO: now also R47.1; no longer R51.1
- net UTS3_TRIG: now also R44.1; no longer R48.1
- net UTS4-ECHO: now also JP20.3, R53.2; no longer JP21.3, R57.2
- net UTS4-TRIG: now also JP20.2, R52.2; no longer JP21.2, R56.2
- net UTS4_ECHO: now also R53.1; no longer R57.1
- net UTS4_TRIG: now also R52.1; no longer R56.1
- net VCC: now also D3.C, D4.A, JP5.1, JP5.3, JP5.5, JP5.7, JP57.2; no longer D1.C, D2.A, JP55.2, JP6.1, JP6.3, JP6.5, JP6.7
- net VUSB: now also D2.A, D7.A, D8.A, JP32.1, R70.2; no longer D3.A, D33.A, D6.A, JP33.1, R75.2
- net VUSB_DET: now also R70.1, R71.2; no longer R75.1, R76.2
- net V_BAT/2: now also D9.C1A2; no longer D34.C1A2
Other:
- note added: "IO12/TDI on ESP32 has internal pull-down during releasing EN, so we need to switch-off the transistor to disconnect pull/up R64."
- note removed: "IO12/TDI on ESP32 has internal pull-down during releasing EN, so we need to switch-off the transistor to disconnect pull/up R69."
- moved on the sheet: D1, D15, D17, D18, D19, D2, D21, D3, D4, D5, D6, JP11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

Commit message: hw: fix value of R74
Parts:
- R74: value 100k -> 330R
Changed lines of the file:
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@@
 <part name="GND164" library="Supply" deviceset="GND" device=""/>
 <part name="GND165" library="Supply" deviceset="GND" device=""/>
-<part name="R74" library="rcl_upravena" deviceset="R-EU_" device="R0402" value="100k"/>
+<part name="R74" library="rcl_upravena" deviceset="R-EU_" device="R0402" value="330R"/>
 <part name="P+43" library="Supply" deviceset="VCC" device=""/>
 <part name="X3" library="con-molex" library_urn="urn:adsk.eagle:library:165" deviceset="52559-3092" device="" package3d_urn="urn:adsk.eagle:package:8078603/1"/>

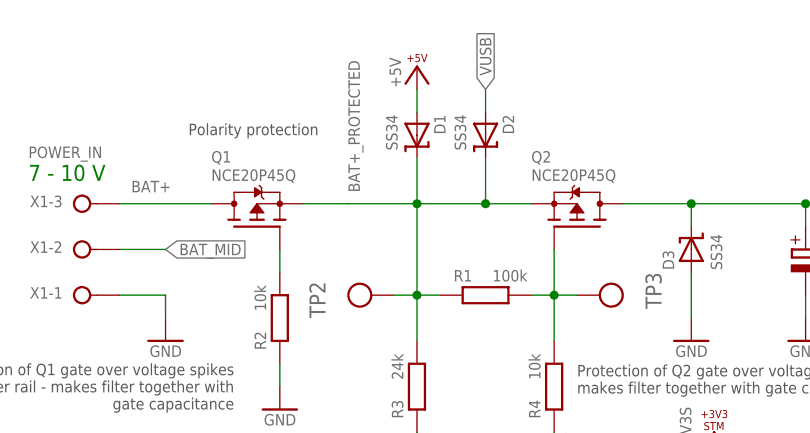
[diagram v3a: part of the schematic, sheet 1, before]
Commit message: hw: replace D1 with smaller one (SS34 -> B5819W)
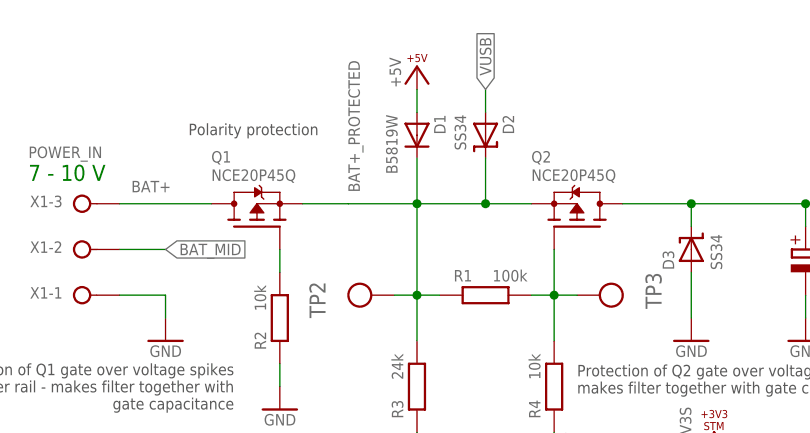
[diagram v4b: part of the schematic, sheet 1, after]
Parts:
- D1: value SS34 -> B5819W; device diode:SHOTTKY-SMA -> diode:DIODE-SOD123
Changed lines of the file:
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@@
 <attribute name="VOLTAGE" value="16V"/>
 </part>
-<part name="D1" library="diode" deviceset="SHOTTKY" device="-SMA" value="SS34"/>
+<part name="D1" library="diode" deviceset="DIODE" device="-SOD123" value="B5819W"/>
 <part name="P+45" library="Supply" deviceset="+5V" device=""/>
 <part name="D2" library="diode" deviceset="SHOTTKY" device="-SMA" value="SS34"/>
@@
 <attribute name="VOLTAGE" x="121.158" y="160.02" size="1.27" layer="96" rot="R90"/>
 </instance>
-<instance part="D1" gate="G$1" x="88.9" y="215.9" smashed="yes" rot="R270">
+<instance part="D1" gate="1" x="88.9" y="215.9" smashed="yes" rot="R270">
 <attribute name="NAME" x="90.805" y="218.186" size="1.27" layer="95" rot="R270"/>
 <attribute name="VALUE" x="86.741" y="218.186" size="1.27" layer="96" rot="MR270"/>
@@
 <pinref part="TP2" gate="G$1" pin="TP"/>
 <wire x1="86.36" y1="198.12" x2="88.9" y2="198.12" width="0.1524" layer="91"/>
-<pinref part="D1" gate="G$1" pin="C"/>
+<pinref part="D1" gate="1" pin="C"/>
 <wire x1="88.9" y1="213.36" x2="88.9" y2="208.28" width="0.1524" layer="91"/>
 <pinref part="D2" gate="G$1" pin="C"/>
@@
 <segment>
 <pinref part="P+45" gate="1" pin="+5V"/>
-<pinref part="D1" gate="G$1" pin="A"/>
+<pinref part="D1" gate="1" pin="A"/>
 <wire x1="88.9" y1="220.98" x2="88.9" y2="218.44" width="0.1524" layer="91"/>
 </segment>
